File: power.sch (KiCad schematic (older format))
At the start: 28 parts, among them U11 MIC5356-SGYMME, U4 5M1270ZT144C5N

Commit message: component placement
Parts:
- U4: symbol CPLD_Altera:5M1270ZT144C5N -> rc2014_max_v-rescue:5M1270ZT144C5N-CPLD_Altera
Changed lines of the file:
@@
 $Descr A4 11693 8268
 encoding utf-8
-Sheet 5 6
+Sheet 6 6
 Title ""
 Date ""
@@
 Connection ~ 5840 3470
 $Comp
-L CPLD_Altera:5M1270ZT144C5N U4
+L rc2014_max_v-rescue:5M1270ZT144C5N-CPLD_Altera U4
 U 7 1 5D3988D8
 P 6060 1940
+AR Path="/5D3988D8" Ref="U4"  Part="7"
+AR Path="/5D2A5E4A/5D3988D8" Ref="U4"  Part="7"
 F 0 "U4" H 6918 1321 50  0000 L CNN
 F 1 "5M1270ZT144C5N" H 6918 1230 50  0000 L CNN

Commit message: organized bypass caps
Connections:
- wire segments 100 -> 103
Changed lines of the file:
@@
 L power:+3V3 #PWR?
 U 1 1 5D3A9E6E
-P 6260 1680
+P 5890 1680
 AR Path="/5D3A9E6E" Ref="#PWR?"  Part="1"
 AR Path="/5D2A5E4A/5D3A9E6E" Ref="#PWR065"  Part="1"
-F 0 "#PWR065" H 6260 1530 50  0001 C CNN
-F 1 "+3V3" V 6275 1808 50  0000 L CNN
-F 2 "" H 6260 1680 50  0001 C CNN
-F 3 "" H 6260 1680 50  0001 C CNN
-	1    6260 1680
+F 0 "#PWR065" H 5890 1530 50  0001 C CNN
+F 1 "+3V3" V 5905 1808 50  0000 L CNN
+F 2 "" H 5890 1680 50  0001 C CNN
+F 3 "" H 5890 1680 50  0001 C CNN
+	1    5890 1680
 	1    0    0    -1
 $EndComp
@@
 	6480 3470 6580 3470
 Connection ~ 6480 3470
-Connection ~ 6350 1740
 Wire Wire Line
 	6380 3470 6480 3470
@@
 Connection ~ 6160 3470
 Wire Wire Line
-	6660 1740 6760 1740
-Connection ~ 6660 1740
+	6660 1740 6710 1740
 Wire Wire Line
 	6050 3470 6100 3470
 Connection ~ 6050 3470
 Wire Wire Line
-	5840 1740 5940 1740
-Connection ~ 5940 1740
-Wire Wire Line
-	6190 1740 6260 1740
-Connection ~ 6190 1740
+	5840 1740 5890 1740
 Wire Wire Line
 	5550 3470 5670 3470
 Connection ~ 5670 3470
 Wire Wire Line
-	6090 1740 6190 1740
-Wire Wire Line
-	5940 1740 6090 1740
-Connection ~ 6090 1740
+	6090 1740 6130 1740
 Wire Wire Line
 	6690 3470 6790 3470
@@
 Connection ~ 5940 3470
 Wire Wire Line
-	6450 1740 6660 1740
-Wire Wire Line
-	6350 1740 6450 1740
-Connection ~ 6450 1740
+	6350 1740 6390 1740
 Wire Wire Line
 	5840 3470 5940 3470
@@
 $EndComp
 Wire Wire Line
-	6260 1680 6260 1740
-Connection ~ 6260 1740
-Wire Wire Line
-	6260 1740 6350 1740
+	5890 1680 5890 1740
 Wire Wire Line
 	6100 3470 6100 3550
@@
 Wire Wire Line
 	1670 4980 2090 4980
+Connection ~ 5890 1740
+Wire Wire Line
+	5890 1740 5940 1740
+$Comp
+L power:+3V3 #PWR?
+U 1 1 5D01A953
+P 6130 1680
+AR Path="/5D01A953" Ref="#PWR?"  Part="1"
+AR Path="/5D2A5E4A/5D01A953" Ref="#PWR091"  Part="1"
+F 0 "#PWR091" H 6130 1530 50  0001 C CNN
+F 1 "+3V3" V 6145 1808 50  0000 L CNN
+F 2 "" H 6130 1680 50  0001 C CNN
+F 3 "" H 6130 1680 50  0001 C CNN
+	1    6130 1680
+	1    0    0    -1
+$EndComp
+Wire Wire Line
+	6130 1680 6130 1740
+Connection ~ 6130 1740
+Wire Wire Line
+	6130 1740 6190 1740
+$Comp
+L power:+3V3 #PWR?
+U 1 1 5D02A315
+P 6390 1680
+AR Path="/5D02A315" Ref="#PWR?"  Part="1"
+AR Path="/5D2A5E4A/5D02A315" Ref="#PWR092"  Part="1"
+F 0 "#PWR092" H 6390 1530 50  0001 C CNN
+F 1 "+3V3" V 6405 1808 50  0000 L CNN
+F 2 "" H 6390 1680 50  0001 C CNN
+F 3 "" H 6390 1680 50  0001 C CNN
+	1    6390 1680
+	1    0    0    -1
+$EndComp
+Wire Wire Line
+	6390 1680 6390 1740
+Connection ~ 6390 1740
+Wire Wire Line
+	6390 1740 6450 1740
+$Comp
+L power:+3V3 #PWR?
+U 1 1 5D0321C3
+P 6710 1680
+AR Path="/5D0321C3" Ref="#PWR?"  Part="1"
+AR Path="/5D2A5E4A/5D0321C3" Ref="#PWR093"  Part="1"
+F 0 "#PWR093" H 6710 1530 50  0001 C CNN
+F 1 "+3V3" V 6725 1808 50  0000 L CNN
+F 2 "" H 6710 1680 50  0001 C CNN
+F 3 "" H 6710 1680 50  0001 C CNN
+	1    6710 1680
+	1    0    0    -1
+$EndComp
+Wire Wire Line
+	6710 1680 6710 1740
+Connection ~ 6710 1740
+Wire Wire Line
+	6710 1740 6760 1740
 $EndSCHEMATC

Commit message: fixed errors, connected all pins, switched to 4 layers
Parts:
- removed C10, C11, C12, C13, C14, C3, C4, C5, C6, C7, C8, C9: 100nF, Capacitor_SMD:C_0603_1608Metric_Pad1.05x0.95mm_HandSolder, symbol Device:C
- removed U4: 5M1270ZT144C5N, QFP50P2200X2200X155-144N, symbol rc2014_max_v-rescue:5M1270ZT144C5N-CPLD_Altera
- added U11: 5M1270ZT144C5N, Package_QFP:TQFP-144_20x20mm_P0.5mm, symbol CPLD_Altera:5M1270ZT144C5N
- renumbered C15 to C42, C48 to C44, C36 to C45, C37 to C46, C38 to C47, C39 to C48, C40 to C49, C41 to C50, C42 to C51, C44 to C52, C45 to C53, C46 to C54, C47 to C55, U11 to U18
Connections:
- net labels added: 1V8, 3V3
- net labels removed: +1V8, +3V3, +5V
- wire segments 103 -> 76

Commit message: consolidated power supply
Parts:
- added JP2: Jumper_3_Bridged12, Connector_PinHeader_2.54mm:PinHeader_1x03_P2.54mm_Vertical, symbol Jumper:Jumper_3_Bridged12
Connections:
- net labels added: 5V_R, 5V_U
- wire segments 76 -> 77
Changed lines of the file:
@@
 	1    0    0    -1
 $EndComp
-Wire Wire Line
-	2950 3310 3090 3310
 $Comp
 L rc2014_max_v-rescue:MIC5356-SGYMME-Regulator_Linear U?
@@
 Wire Wire Line
 	2620 3510 2620 3440
-Wire Wire Line
-	2620 3440 3090 3440
 Wire Wire Line
 	5530 1680 5530 1740
@@
 	2540 3440 2620 3440
 Connection ~ 2620 3440
-Text GLabel 3090 3310 2    50   Output ~ 0
+Text GLabel 3260 3310 2    50   Output ~ 0
 3V3
-Text GLabel 3090 3440 2    50   Output ~ 0
+Text GLabel 3260 3440 2    50   Output ~ 0
 1V8
 Text GLabel 2090 4920 1    50   Output ~ 0
@@
 Wire Wire Line
 	5380 1740 5480 1740
-Wire Wire Line
-	5530 1740 5590 1740
 Connection ~ 5480 1740
-Wire Wire Line
-	5480 1740 5530 1740
 Connection ~ 5590 1740
 Wire Wire Line
 	5590 1740 5700 1740
+Wire Wire Line
+	2950 3310 3260 3310
+Wire Wire Line
+	2620 3440 3260 3440
+Wire Wire Line
+	2140 1440 2140 1540
+Text GLabel 2140 1660 3    50   Output ~ 0
+5V
+$Comp
+L Jumper:Jumper_3_Bridged12 JP?
+U 1 1 5D02332B
+P 2140 1290
+AR Path="/5D02332B" Ref="JP?"  Part="1"
+AR Path="/5CF9C1ED/5D02332B" Ref="JP?"  Part="1"
+AR Path="/5D2A5E4A/5D02332B" Ref="JP2"  Part="1"
+F 0 "JP2" H 2140 1494 50  0000 C CNN
+F 1 "Jumper_3_Bridged12" H 2140 1403 50  0000 C CNN
+F 2 "Connector_PinHeader_2.54mm:PinHeader_1x03_P2.54mm_Vertical" H 2140 1290 50  0001 C CNN
+F 3 "~" H 2140 1290 50  0001 C CNN
+	1    2140 1290
+	1    0    0    -1
+$EndComp
+$Comp
+L power:PWR_FLAG #FLG?
+U 1 1 5D023331
+P 2140 1540
+AR Path="/5CF9C1ED/5D023331" Ref="#FLG?"  Part="1"
+AR Path="/5D2A5E4A/5D023331" Ref="#FLG0101"  Part="1"
+F 0 "#FLG0101" H 2140 1615 50  0001 C CNN
+F 1 "PWR_FLAG" H 2140 1713 50  0000 C CNN
+F 2 "" H 2140 1540 50  0001 C CNN
+F 3 "~" H 2140 1540 50  0001 C CNN
+	1    2140 1540
+	0    -1   -1   0
+$EndComp
+Connection ~ 2140 1540
+Wire Wire Line
+	2140 1540 2140 1660
+Text GLabel 1800 1290 0    50   Input ~ 0
+5V_U
+Wire Wire Line
+	1800 1290 1890 1290
+Text GLabel 2390 1290 2    50   Input ~ 0
+5V_R
 $EndSCHEMATC

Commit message: Updated BOM
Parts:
- C42, C44, C45, C46, C47, C48, C49, C50, C51, C52, C53, C54, C55: MFR KEMET -> Taiyo Yuden; MPN C0805C104K4RACTU -> TMK107BJ104KA-T; SPN 80-C0805C104K4R -> (none)
- C43: MFR KEMET -> Taiyo Yuden; MPN C0805C104K4RACTU -> JMK107BJ225KA-T; SPN 80-C0805C104K4R -> (none)
- JP2: footprint Connector_PinHeader_2.54mm:PinHeader_1x03_P2.54mm_Vertical -> Connector_PinHeader_2.54mm:PinHeader_1x03_P2.54mm_Horizontal
- U11: symbol CPLD_Altera:5M1270ZT144C5N -> rc2014_max_v-rescue:5M1270ZT144C5N-CPLD_Altera; MFR (none) -> Intel; MPN (none) -> 5M1270ZT144C5N; Manufacturer_Name Intel -> (none); SPR (none) -> Mouser
- U18: MFR (none) -> Microchip Technology; MPN (none) -> MIC5356-SGYMME; SPR (none) -> Mouser

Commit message: updated descriptions and part #'s
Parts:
- C42, C44, C45, C46, C47, C48, C49, C50, C51, C52, C53, C54, C55: Description (none) -> Multilayer Ceramic Capacitors MLCC - SMD/SMT 0.1uF 25V X5R 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; SPN (none) -> 963-TMK107BJ104KA-T; SPURL https://www.mouser.com/ProductDetail/KEMET/C0805C104K4RACTU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 -> https://www.mouser.com/ProductDetail/963-TMK107BJ104KA-T
- C43: Description (none) -> Multilayer Ceramic Capacitors MLCC - SMD/SMT 2.2uF 6.3V X5R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; SPN (none) -> 963-JMK107BJ225KA-T; SPURL https://www.mouser.com/ProductDetail/KEMET/C0805C104K4RACTU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 -> https://www.mouser.com/ProductDetail/963-JMK107BJ225KA-T
- U11: SPN (none) -> 989-5M1270ZT144C5N; SPURL (none) -> https://www.mouser.com/ProductDetail/989-5M1270ZT144C5N
- U18: Description (none) -> LDO Voltage Regulators Dual 500mA uCap Low Dropout, Micropo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; SPN (none) -> 998-MIC5356-SGYMME; SPURL (none) -> https://www.mouser.com/ProductDetail/998-MIC5356-SGYMME

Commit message: moved things around to improve routing, fixed power plane
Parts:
- JP2: footprint Connector_PinHeader_2.54mm:PinHeader_1x03_P2.54mm_Horizontal -> Connector_PinHeader_2.54mm:PinHeader_1x03_P2.54mm_Vertical
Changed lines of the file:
@@
 F 0 "JP2" H 2140 1494 50  0000 C CNN
 F 1 "Jumper_3_Bridged12" H 2140 1403 50  0000 C CNN
-F 2 "Connector_PinHeader_2.54mm:PinHeader_1x03_P2.54mm_Horizontal" H 2140 1290 50  0001 C CNN
+F 2 "Connector_PinHeader_2.54mm:PinHeader_1x03_P2.54mm_Vertical" H 2140 1290 50  0001 C CNN
 F 3 "~" H 2140 1290 50  0001 C CNN
 	1    2140 1290

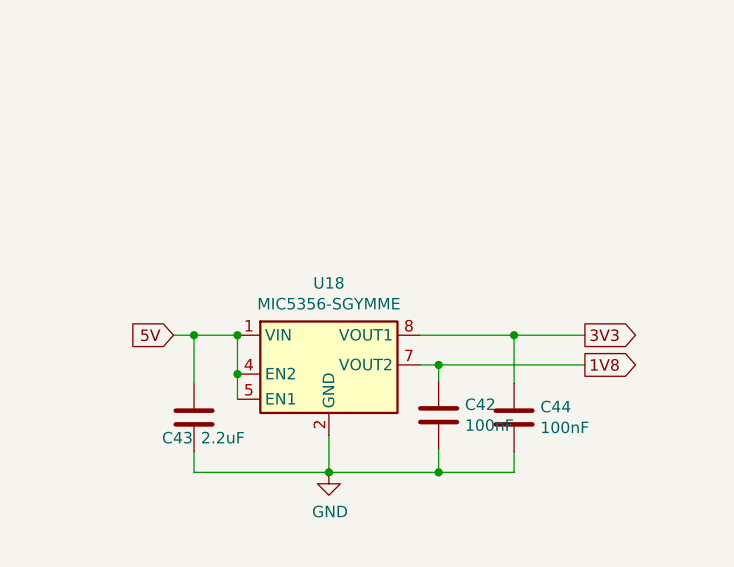
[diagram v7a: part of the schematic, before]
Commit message: replaced some global pins with hierarchical sheet pins
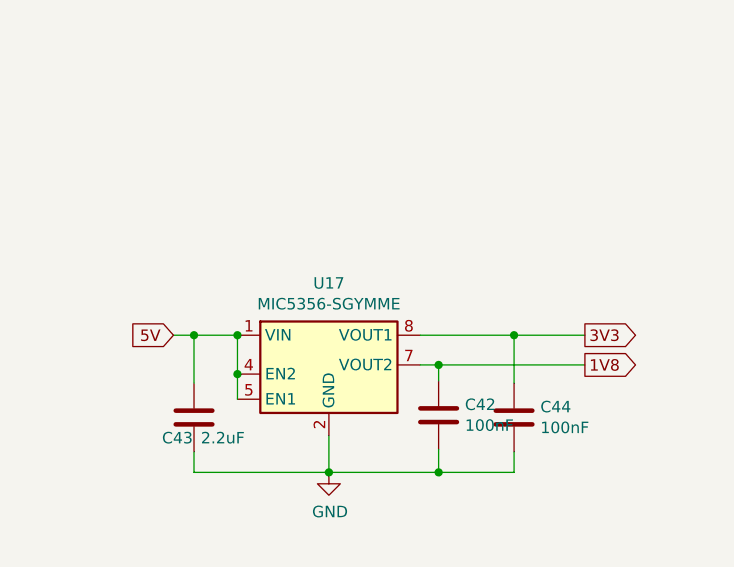
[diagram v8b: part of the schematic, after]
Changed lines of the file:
@@
 $Descr A4 11693 8268
 encoding utf-8
-Sheet 6 6
+Sheet 5 6
 Title ""
 Date ""
@@
 AR Path="/5D2BC417" Ref="C?"  Part="1"
 AR Path="/5D2A5E4A/5D2BC417" Ref="C43"  Part="1"
+AR Path="/5CFABACD/5D2103A8/5D2BC417" Ref="C43"  Part="1"
 F 0 "C43" H 1410 3580 50  0000 L CNN
 F 1 "2.2uF" H 1580 3580 50  0000 L CNN
@@
 AR Path="/5D2BC422" Ref="C?"  Part="1"
 AR Path="/5D2A5E4A/5D2BC422" Ref="C42"  Part="1"
+AR Path="/5CFABACD/5D2103A8/5D2BC422" Ref="C42"  Part="1"
 F 0 "C42" H 2735 3706 50  0000 L CNN
 F 1 "100nF" H 2735 3615 50  0000 L CNN
@@
 AR Path="/5D2BC430" Ref="C?"  Part="1"
 AR Path="/5D2A5E4A/5D2BC430" Ref="C44"  Part="1"
+AR Path="/5CFABACD/5D2103A8/5D2BC430" Ref="C44"  Part="1"
 F 0 "C44" H 3065 3716 50  0000 L CNN
 F 1 "100nF" H 3065 3625 50  0000 L CNN
@@
 AR Path="/5D2BC445" Ref="U?"  Part="1"
 AR Path="/5D2A5E4A/5D2BC445" Ref="U18"  Part="1"
-F 0 "U18" H 2140 3817 50  0000 C CNN
+AR Path="/5CFABACD/5D2103A8/5D2BC445" Ref="U17"  Part="1"
+F 0 "U17" H 2140 3817 50  0000 C CNN
 F 1 "MIC5356-SGYMME" H 2140 3726 50  0000 C CNN
 F 2 "Package_SO:MSOP-8-1EP_3x3mm_P0.65mm_EP2.5x3mm_Mask1.73x2.36mm_ThermalVias" H 3540 3200 50  0001 C CNN
@@
 AR Path="/5CFABACD/5D2BC45C" Ref="#PWR?"  Part="1"
 AR Path="/5D2A5E4A/5D2BC45C" Ref="#PWR0100"  Part="1"
-F 0 "#PWR0100" H 2140 3660 50  0001 C CNN
+AR Path="/5CFABACD/5D2103A8/5D2BC45C" Ref="#PWR020"  Part="1"
+F 0 "#PWR020" H 2140 3660 50  0001 C CNN
 F 1 "GND" H 2145 3737 50  0000 C CNN
 F 2 "" H 2140 3910 50  0001 C CNN
@@
 AR Path="/5CFABACD/5D3ADBA3" Ref="#PWR?"  Part="1"
 AR Path="/5D2A5E4A/5D3ADBA3" Ref="#PWR099"  Part="1"
-F 0 "#PWR099" H 6100 3300 50  0001 C CNN
+AR Path="/5CFABACD/5D2103A8/5D3ADBA3" Ref="#PWR019"  Part="1"
+F 0 "#PWR019" H 6100 3300 50  0001 C CNN
 F 1 "GND" H 6105 3377 50  0000 C CNN
 F 2 "" H 6100 3550 50  0001 C CNN
@@
 AR Path="/5D3E146F" Ref="C?"  Part="1"
 AR Path="/5D2A5E4A/5D3E146F" Ref="C45"  Part="1"
+AR Path="/5CFABACD/5D2103A8/5D3E146F" Ref="C45"  Part="1"
 F 0 "C45" H 985 5176 50  0000 L CNN
 F 1 "100nF" H 985 5085 50  0000 L CNN
@@
 AR Path="/5D3E147A" Ref="C?"  Part="1"
 AR Path="/5D2A5E4A/5D3E147A" Ref="C46"  Part="1"
+AR Path="/5CFABACD/5D2103A8/5D3E147A" Ref="C46"  Part="1"
 F 0 "C46" H 1355 5176 50  0000 L CNN
 F 1 "100nF" H 1355 5085 50  0000 L CNN
@@
 AR Path="/5CFABACD/5D3E1487" Ref="#PWR?"  Part="1"
 AR Path="/5D2A5E4A/5D3E1487" Ref="#PWR0101"  Part="1"
-F 0 "#PWR0101" H 2090 5110 50  0001 C CNN
+AR Path="/5CFABACD/5D2103A8/5D3E1487" Ref="#PWR023"  Part="1"
+F 0 "#PWR023" H 2090 5110 50  0001 C CNN
 F 1 "GND" H 2095 5187 50  0000 C CNN
 F 2 "" H 2090 5360 50  0001 C CNN
@@
 AR Path="/5D3E1493" Ref="C?"  Part="1"
 AR Path="/5D2A5E4A/5D3E1493" Ref="C48"  Part="1"
+AR Path="/5CFABACD/5D2103A8/5D3E1493" Ref="C48"  Part="1"
 F 0 "C48" H 2205 5176 50  0000 L CNN
 F 1 "100nF" H 2205 5085 50  0000 L CNN
@@
 AR Path="/5D3E149E" Ref="C?"  Part="1"
 AR Path="/5D2A5E4A/5D3E149E" Ref="C47"  Part="1"
+AR Path="/5CFABACD/5D2103A8/5D3E149E" Ref="C47"  Part="1"
 F 0 "C47" H 1785 5176 50  0000 L CNN
 F 1 "100nF" H 1785 5085 50  0000 L CNN
@@
 AR Path="/5D3E14A9" Ref="C?"  Part="1"
 AR Path="/5D2A5E4A/5D3E14A9" Ref="C50"  Part="1"
+AR Path="/5CFABACD/5D2103A8/5D3E14A9" Ref="C50"  Part="1"
 F 0 "C50" H 3005 5176 50  0000 L CNN
 F 1 "100nF" H 3005 5085 50  0000 L CNN
@@
 AR Path="/5D3E14B4" Ref="C?"  Part="1"
 AR Path="/5D2A5E4A/5D3E14B4" Ref="C49"  Part="1"
+AR Path="/5CFABACD/5D2103A8/5D3E14B4" Ref="C49"  Part="1"
 F 0 "C49" H 2585 5176 50  0000 L CNN
 F 1 "100nF" H 2585 5085 50  0000 L CNN
@@
 AR Path="/5D3E14CF" Ref="C?"  Part="1"
 AR Path="/5D2A5E4A/5D3E14CF" Ref="C52"  Part="1"
+AR Path="/5CFABACD/5D2103A8/5D3E14CF" Ref="C52"  Part="1"
 F 0 "C52" H 1465 6236 50  0000 L CNN
 F 1 "100nF" H 1465 6145 50  0000 L CNN
@@
 AR Path="/5D3E14DA" Ref="C?"  Part="1"
 AR Path="/5D2A5E4A/5D3E14DA" Ref="C53"  Part="1"
+AR Path="/5CFABACD/5D2103A8/5D3E14DA" Ref="C53"  Part="1"
 F 0 "C53" H 1815 6236 50  0000 L CNN
 F 1 "100nF" H 1815 6145 50  0000 L CNN
@@
 AR Path="/5CFABACD/5D3E14E1" Ref="#PWR?"  Part="1"
 AR Path="/5D2A5E4A/5D3E14E1" Ref="#PWR0102"  Part="1"
-F 0 "#PWR0102" H 1900 6170 50  0001 C CNN
+AR Path="/5CFABACD/5D2103A8/5D3E14E1" Ref="#PWR025"  Part="1"
+F 0 "#PWR025" H 1900 6170 50  0001 C CNN
 F 1 "GND" H 1905 6247 50  0000 C CNN
 F 2 "" H 1900 6420 50  0001 C CNN
@@
 AR Path="/5D3E14ED" Ref="C?"  Part="1"
 AR Path="/5D2A5E4A/5D3E14ED" Ref="C54"  Part="1"
+AR Path="/5CFABACD/5D2103A8/5D3E14ED" Ref="C54"  Part="1"
 F 0 "C54" H 2205 6236 50  0000 L CNN
 F 1 "100nF" H 2205 6145 50  0000 L CNN
@@
 AR Path="/5D3E14F8" Ref="C?"  Part="1"
 AR Path="/5D2A5E4A/5D3E14F8" Ref="C55"  Part="1"
+AR Path="/5CFABACD/5D2103A8/5D3E14F8" Ref="C55"  Part="1"
 F 0 "C55" H 2645 6236 50  0000 L CNN
 F 1 "100nF" H 2645 6145 50  0000 L CNN
@@
 AR Path="/5D3E1517" Ref="C?"  Part="1"
 AR Path="/5D2A5E4A/5D3E1517" Ref="C51"  Part="1"
+AR Path="/5CFABACD/5D2103A8/5D3E1517" Ref="C51"  Part="1"
 F 0 "C51" H 3385 5176 50  0000 L CNN
 F 1 "100nF" H 3385 5085 50  0000 L CNN
@@
 AR Path="/5D1CBE97" Ref="U11"  Part="7"
 AR Path="/5D2A5E4A/5D1CBE97" Ref="U11"  Part="7"
+AR Path="/5CFABACD/5D2103A8/5D1CBE97" Ref="U11"  Part="7"
 F 0 "U11" H 6918 1321 50  0000 L CNN
 F 1 "5M1270ZT144C5N" H 6918 1230 50  0000 L CNN
@@
 AR Path="/5CF9C1ED/5D02332B" Ref="JP?"  Part="1"
 AR Path="/5D2A5E4A/5D02332B" Ref="JP2"  Part="1"
+AR Path="/5CFABACD/5D2103A8/5D02332B" Ref="JP2"  Part="1"
 F 0 "JP2" H 2140 1494 50  0000 C CNN
 F 1 "Jumper_3_Bridged12" H 2140 1403 50  0000 C CNN
@@
 AR Path="/5CF9C1ED/5D023331" Ref="#FLG?"  Part="1"
 AR Path="/5D2A5E4A/5D023331" Ref="#FLG0101"  Part="1"
-F 0 "#FLG0101" H 2140 1615 50  0001 C CNN
+AR Path="/5CFABACD/5D2103A8/5D023331" Ref="#FLG05"  Part="1"
+F 0 "#FLG05" H 2140 1615 50  0001 C CNN
 F 1 "PWR_FLAG" H 2140 1713 50  0000 C CNN
 F 2 "" H 2140 1540 50  0001 C CNN
